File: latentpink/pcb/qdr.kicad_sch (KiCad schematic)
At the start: 68 parts, among them U2 XC7K160T-2FBG484C, U28 IS25WP256D-JLLE, U3 CY7C2245KV18-450BZXI

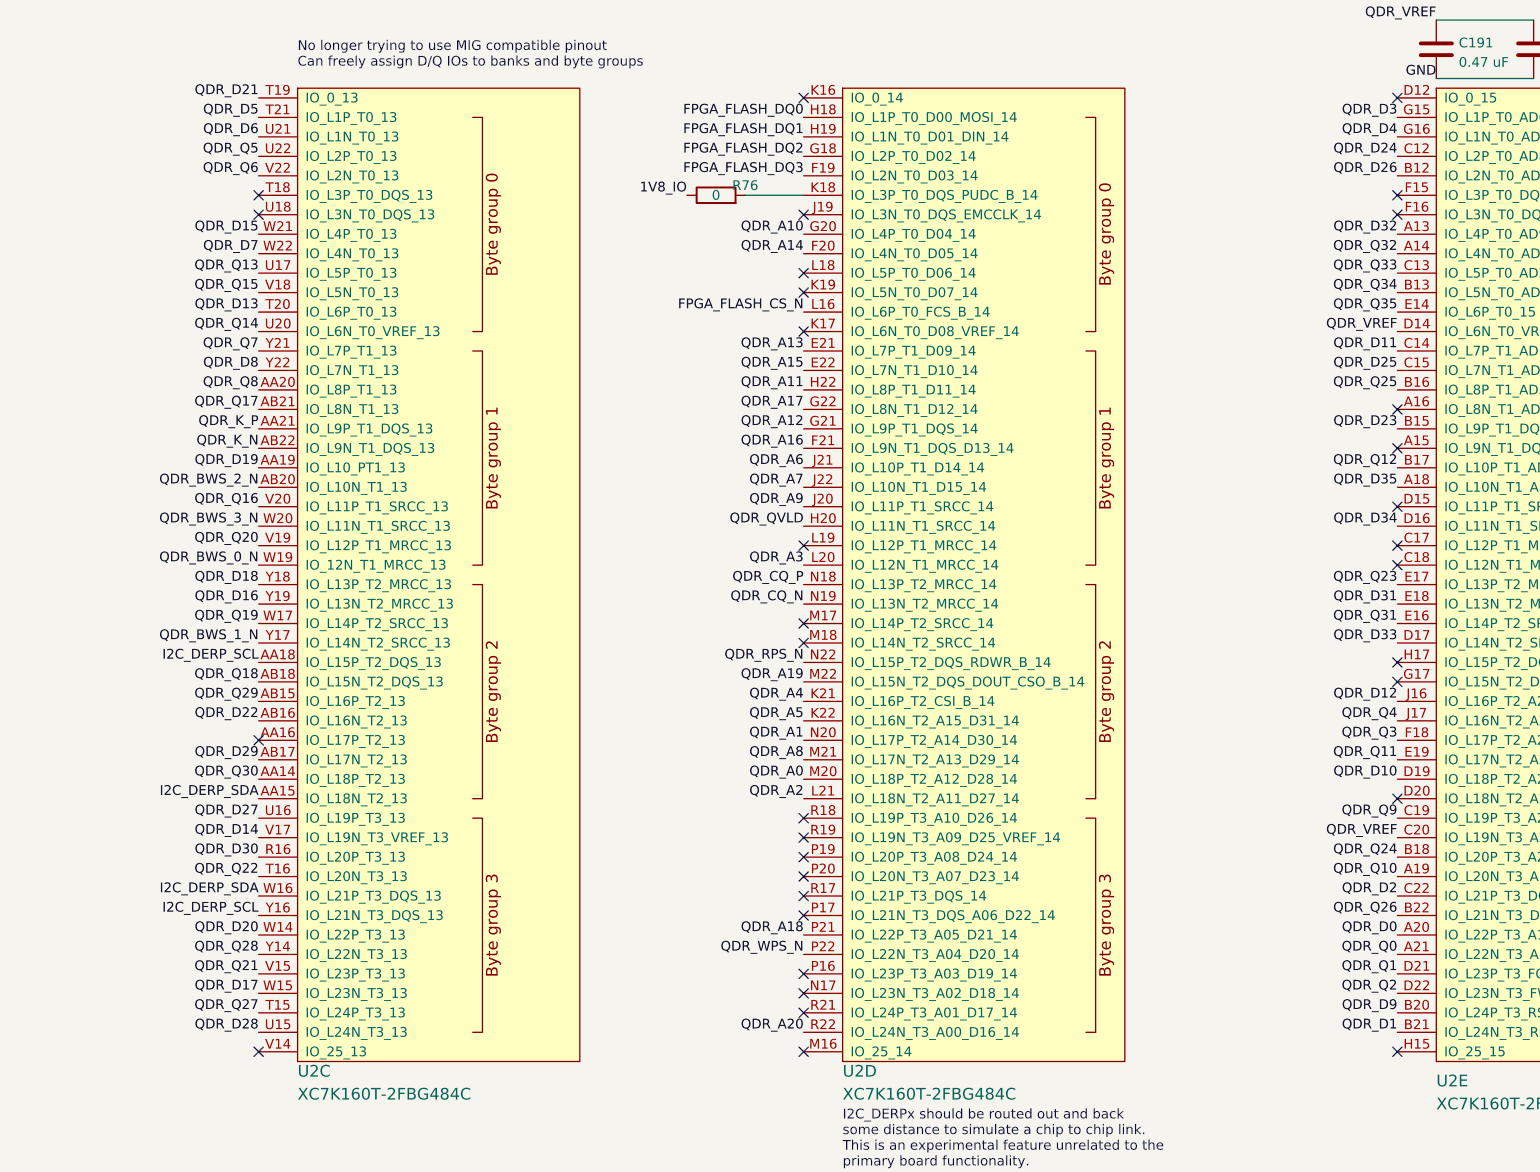
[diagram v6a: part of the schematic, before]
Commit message: Continued initial QDR routing
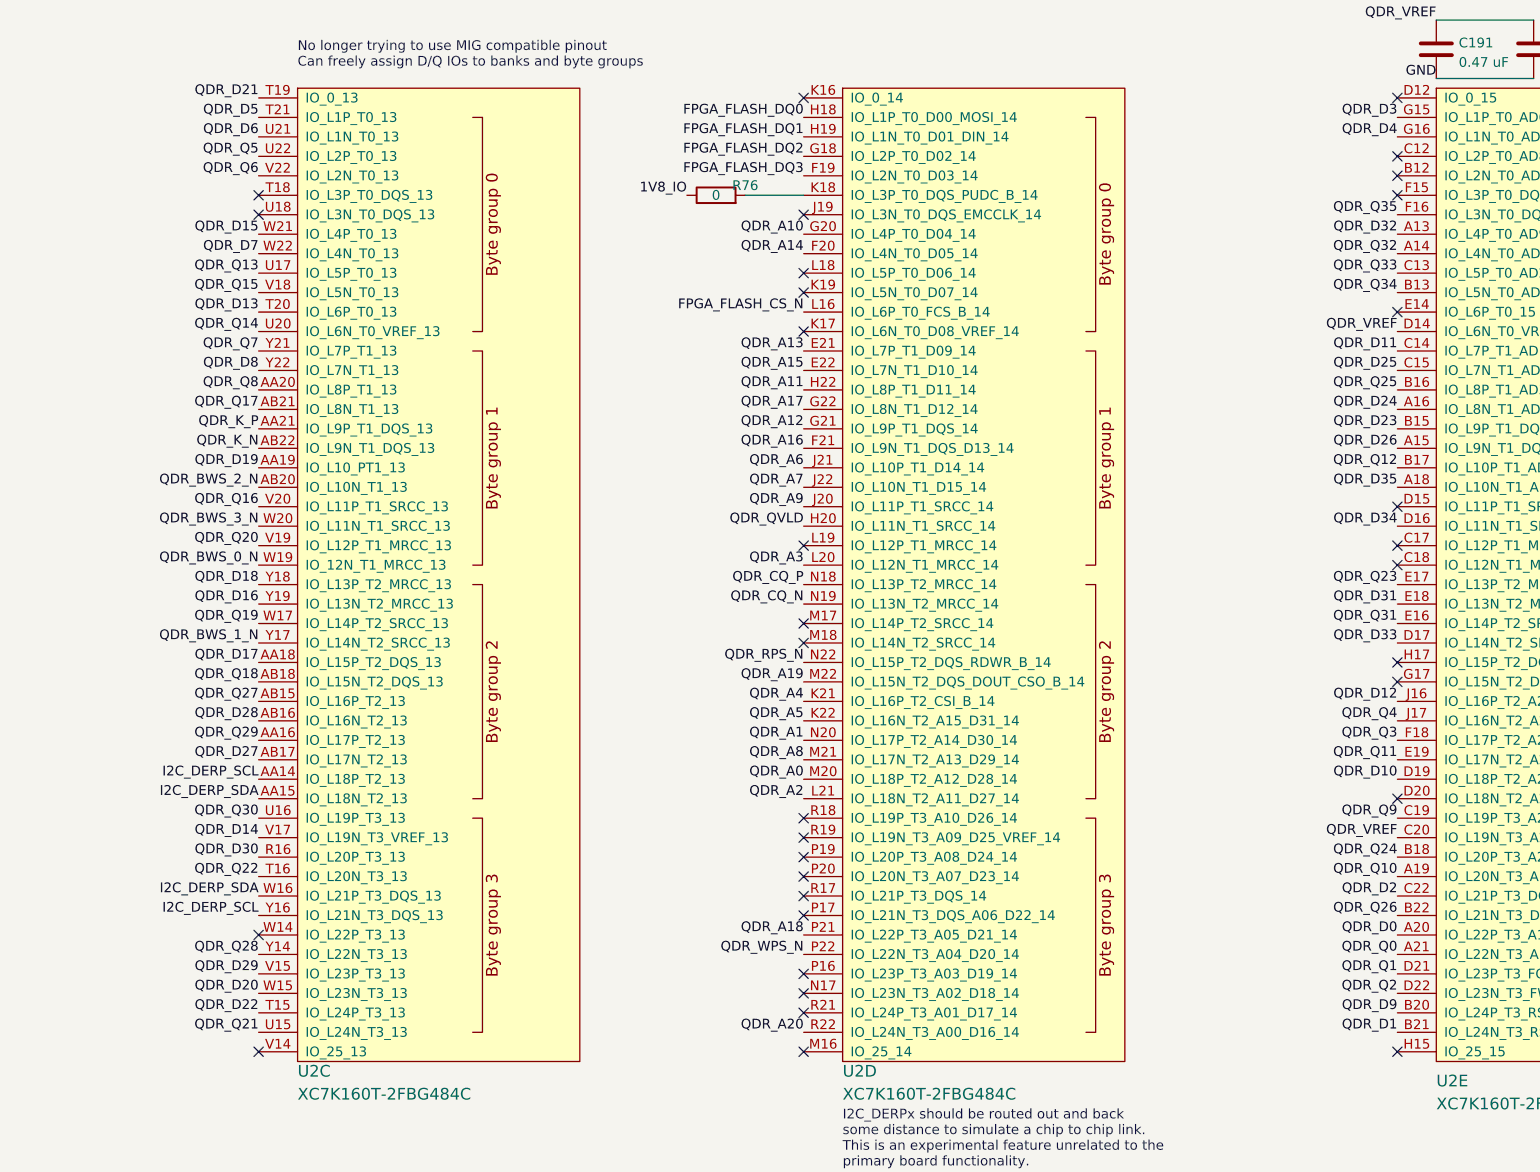
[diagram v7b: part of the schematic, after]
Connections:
- net I2C_DERP_SCL: now also U2.AA14 (IO_L18P_T2_13); no longer U2.AA18 (IO_L15P_T2_DQS_13)
- net QDR_D17: now also U2.AA18 (IO_L15P_T2_DQS_13); no longer U2.W15 (IO_L23N_T3_13)
- net QDR_D20: now also U2.W15 (IO_L23N_T3_13); no longer U2.W14 (IO_L22P_T3_13)
- net QDR_D22: now also U2.T15 (IO_L24P_T3_13); no longer U2.AB16 (IO_L16N_T2_13)
- net QDR_D24: now also U2.A16 (IO_L8N_T1_AD3N_15); no longer U2.C12 (IO_L2P_T0_AD8P_15)
- net QDR_D26: now also U2.A15 (IO_L9N_T1_DQS_AD11N_15); no longer U2.B12 (IO_L2N_T0_AD8N_15)
- net QDR_D27: now also U2.AB17 (IO_L17N_T2_13); no longer U2.U16 (IO_L19P_T3_13)
- net QDR_D28: now also U2.AB16 (IO_L16N_T2_13); no longer U2.U15 (IO_L24N_T3_13)
- net QDR_D29: now also U2.V15 (IO_L23P_T3_13); no longer U2.AB17 (IO_L17N_T2_13)
- net QDR_Q21: now also U2.U15 (IO_L24N_T3_13); no longer U2.V15 (IO_L23P_T3_13)
- net QDR_Q27: now also U2.AB15 (IO_L16P_T2_13); no longer U2.T15 (IO_L24P_T3_13)
- net QDR_Q29: now also U2.AA16 (IO_L17P_T2_13); no longer U2.AB15 (IO_L16P_T2_13)
- net QDR_Q30: now also U2.U16 (IO_L19P_T3_13); no longer U2.AA14 (IO_L18P_T2_13)
- net QDR_Q35: now also U2.F16 (IO_L3N_T0_DQS_AD1N_15); no longer U2.E14 (IO_L6P_T0_15)
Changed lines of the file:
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@@
   (paper "A3")
   (title_block
-    (date "2023-06-01")
+    (date "2023-06-03")
     (rev "0.1")
     (company "Antikernel Labs")
@@
   (no_connect (at 269.24 132.08))
   (no_connect (at 346.71 99.06))
+  (no_connect (at 346.71 33.02))
   (no_connect (at 33.02 181.61))
   (no_connect (at 346.71 25.4))
   (no_connect (at 269.24 83.82))
-  (no_connect (at 346.71 40.64))
   (no_connect (at 346.71 38.1))
   (no_connect (at 269.24 149.86))
@@
   (no_connect (at 346.71 101.6))
   (no_connect (at 346.71 78.74))
-  (no_connect (at 346.71 71.12))
+  (no_connect (at 346.71 53.34))
   (no_connect (at 269.24 55.88))
   (no_connect (at 269.24 25.4))
@@
   (no_connect (at 346.71 149.86))
   (no_connect (at 200.66 264.16))
-  (no_connect (at 346.71 66.04))
   (no_connect (at 269.24 129.54))
   (no_connect (at 33.02 179.07))
@@
   (no_connect (at 269.24 93.98))
   (no_connect (at 269.24 127))
-  (no_connect (at 198.12 109.22))
+  (no_connect (at 346.71 35.56))
+  (no_connect (at 198.12 134.62))
   (wire (pts (xy 88.9 209.55) (xy 101.6 209.55))
     (stroke (width 0) (type default) (color 0 0 0 0))
@@
     (effects (font (size 1.27 1.27)) (justify right bottom))
   )
-  (label "QDR_D20" (at 198.12 134.62 180)
+  (label "QDR_D20" (at 198.12 142.24 180)
     (effects (font (size 1.27 1.27)) (justify right bottom))
   )
@@
     (effects (font (size 1.27 1.27)) (justify right bottom))
   )
-  (label "QDR_D28" (at 198.12 147.32 180)
+  (label "QDR_D28" (at 198.12 106.68 180)
     (effects (font (size 1.27 1.27)) (justify right bottom))
   )
@@
     (effects (font (size 1.27 1.27)) (justify right bottom))
   )
-  (label "QDR_D29" (at 198.12 111.76 180)
+  (label "QDR_D29" (at 198.12 139.7 180)
     (effects (font (size 1.27 1.27)) (justify right bottom))
   )
@@
     (effects (font (size 1.27 1.27)) (justify right bottom))
   )
-  (label "QDR_Q30" (at 198.12 114.3 180)
+  (label "QDR_Q30" (at 198.12 119.38 180)
     (effects (font (size 1.27 1.27)) (justify right bottom))
   )
@@
     (effects (font (size 1.27 1.27)) (justify right bottom))
   )
-  (label "QDR_D17" (at 198.12 142.24 180)
+  (label "QDR_D17" (at 198.12 99.06 180)
     (effects (font (size 1.27 1.27)) (justify right bottom))
   )
@@
     (effects (font (size 1.27 1.27)) (justify right bottom))
   )
-  (label "QDR_D27" (at 198.12 119.38 180)
+  (label "QDR_D27" (at 198.12 111.76 180)
     (effects (font (size 1.27 1.27)) (justify right bottom))
   )
@@
     (effects (font (size 1.27 1.27)) (justify right bottom))
   )
-  (label "QDR_Q29" (at 198.12 104.14 180)
+  (label "QDR_Q29" (at 198.12 109.22 180)
     (effects (font (size 1.27 1.27)) (justify right bottom))
   )
@@
     (effects (font (size 1.27 1.27)) (justify right bottom))
   )
-  (label "QDR_D26" (at 346.71 35.56 180)
+  (label "QDR_D26" (at 346.71 71.12 180)
     (effects (font (size 1.27 1.27)) (justify right bottom))
   )
@@
     (effects (font (size 1.27 1.27)) (justify right bottom))
   )
-  (label "QDR_D24" (at 346.71 33.02 180)
+  (label "QDR_D24" (at 346.71 66.04 180)
     (effects (font (size 1.27 1.27)) (justify right bottom))
   )
@@
     (effects (font (size 1.27 1.27)) (justify right bottom))
   )
-  (label "QDR_Q21" (at 198.12 139.7 180)
+  (label "QDR_Q21" (at 198.12 147.32 180)
     (effects (font (size 1.27 1.27)) (justify right bottom))
   )
@@
     (effects (font (size 1.27 1.27)) (justify right bottom))
   )
-  (label "QDR_Q27" (at 198.12 144.78 180)
+  (label "QDR_Q27" (at 198.12 104.14 180)
     (effects (font (size 1.27 1.27)) (justify right bottom))
   )
@@
     (effects (font (size 1.27 1.27)) (justify right bottom))
   )
-  (label "QDR_D22" (at 198.12 106.68 180)
+  (label "QDR_D22" (at 198.12 144.78 180)
     (effects (font (size 1.27 1.27)) (justify right bottom))
   )
@@
     (effects (font (size 1.27 1.27)) (justify right bottom))
   )
-  (label "QDR_Q35" (at 346.71 53.34 180)
+  (label "QDR_Q35" (at 346.71 40.64 180)
     (effects (font (size 1.27 1.27)) (justify right bottom))
   )
@@
     (effects (font (size 1.27 1.27)) (justify right bottom))
   )
-  (label "I2C_DERP_SCL" (at 198.12 99.06 180)
-    (effects (font (size 1.27 1.27)) (justify right bottom))
-  )
+  (label "I2C_DERP_SCL" (at 198.12 114.3 180)
+    (effects (font (size 1.27 1.27)) (justify right bottom))
+  )

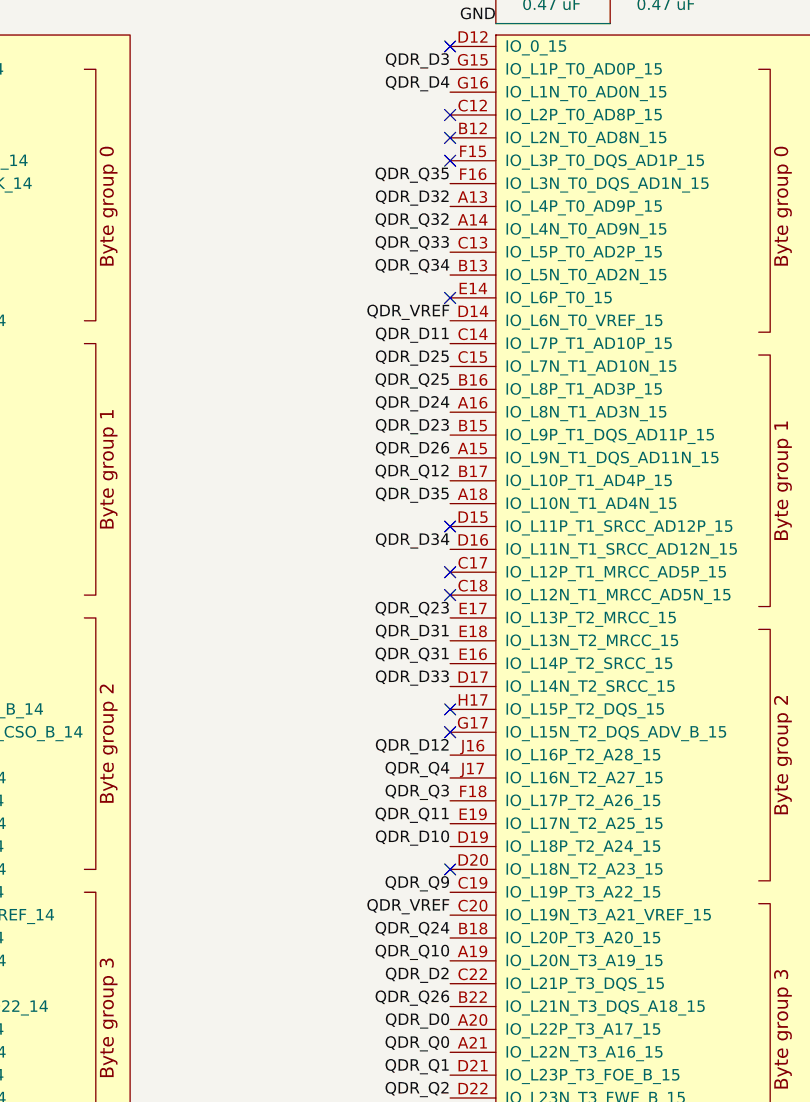
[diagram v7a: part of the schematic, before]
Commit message: Finished initial QDR routing, not length matched. 74 unrouted.
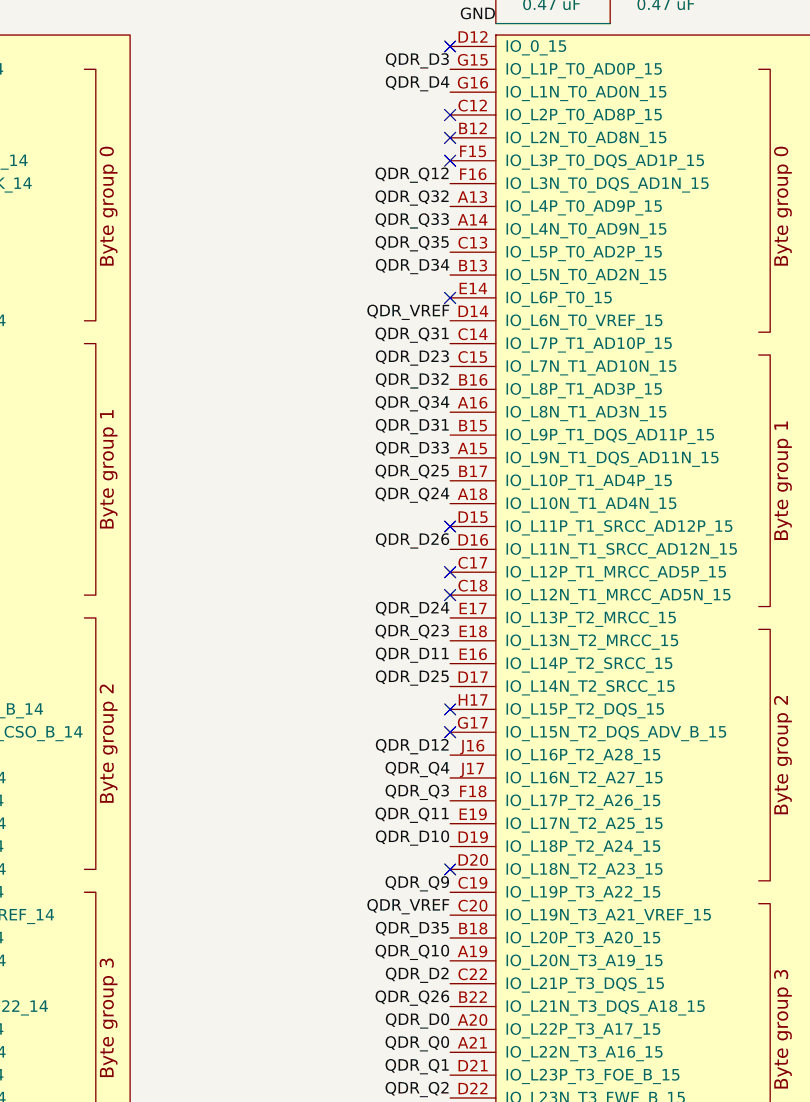
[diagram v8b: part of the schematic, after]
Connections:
- net QDR_D11: now also U2.E16 (IO_L14P_T2_SRCC_15); no longer U2.C14 (IO_L7P_T1_AD10P_15)
- net QDR_D23: now also U2.C15 (IO_L7N_T1_AD10N_15); no longer U2.B15 (IO_L9P_T1_DQS_AD11P_15)
- net QDR_D24: now also U2.E17 (IO_L13P_T2_MRCC_15); no longer U2.A16 (IO_L8N_T1_AD3N_15)
- net QDR_D25: now also U2.D17 (IO_L14N_T2_SRCC_15); no longer U2.C15 (IO_L7N_T1_AD10N_15)
- net QDR_D26: now also U2.D16 (IO_L11N_T1_SRCC_AD12N_15); no longer U2.A15 (IO_L9N_T1_DQS_AD11N_15)
- net QDR_D31: now also U2.B15 (IO_L9P_T1_DQS_AD11P_15); no longer U2.E18 (IO_L13N_T2_MRCC_15)
- net QDR_D32: now also U2.B16 (IO_L8P_T1_AD3P_15); no longer U2.A13 (IO_L4P_T0_AD9P_15)
- net QDR_D33: now also U2.A15 (IO_L9N_T1_DQS_AD11N_15); no longer U2.D17 (IO_L14N_T2_SRCC_15)
- net QDR_D34: now also U2.B13 (IO_L5N_T0_AD2N_15); no longer U2.D16 (IO_L11N_T1_SRCC_AD12N_15)
- net QDR_D35: now also U2.B18 (IO_L20P_T3_A20_15); no longer U2.A18 (IO_L10N_T1_AD4N_15)
- net QDR_Q12: now also U2.F16 (IO_L3N_T0_DQS_AD1N_15); no longer U2.B17 (IO_L10P_T1_AD4P_15)
- net QDR_Q23: now also U2.E18 (IO_L13N_T2_MRCC_15); no longer U2.E17 (IO_L13P_T2_MRCC_15)
- net QDR_Q24: now also U2.A18 (IO_L10N_T1_AD4N_15); no longer U2.B18 (IO_L20P_T3_A20_15)
- net QDR_Q25: now also U2.B17 (IO_L10P_T1_AD4P_15); no longer U2.B16 (IO_L8P_T1_AD3P_15)
- net QDR_Q31: now also U2.C14 (IO_L7P_T1_AD10P_15); no longer U2.E16 (IO_L14P_T2_SRCC_15)
- net QDR_Q32: now also U2.A13 (IO_L4P_T0_AD9P_15); no longer U2.A14 (IO_L4N_T0_AD9N_15)
- net QDR_Q33: now also U2.A14 (IO_L4N_T0_AD9N_15); no longer U2.C13 (IO_L5P_T0_AD2P_15)
- net QDR_Q34: now also U2.A16 (IO_L8N_T1_AD3N_15); no longer U2.B13 (IO_L5N_T0_AD2N_15)
- net QDR_Q35: now also U2.C13 (IO_L5P_T0_AD2P_15); no longer U2.F16 (IO_L3N_T0_DQS_AD1N_15)
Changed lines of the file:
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@@
     (effects (font (size 1.27 1.27)) (justify right bottom))
   )
-  (label "QDR_D31" (at 346.71 91.44 180)
+  (label "QDR_D31" (at 346.71 68.58 180)
     (effects (font (size 1.27 1.27)) (justify right bottom))
   )
@@
     (effects (font (size 1.27 1.27)) (justify right bottom))
   )
-  (label "QDR_D32" (at 346.71 43.18 180)
+  (label "QDR_D32" (at 346.71 63.5 180)
     (effects (font (size 1.27 1.27)) (justify right bottom))
   )
@@
     (effects (font (size 1.27 1.27)) (justify right bottom))
   )
-  (label "QDR_D35" (at 346.71 76.2 180)
+  (label "QDR_D35" (at 346.71 124.46 180)
     (effects (font (size 1.27 1.27)) (justify right bottom))
   )
@@
     (effects (font (size 1.27 1.27)) (justify right bottom))
   )
-  (label "QDR_Q12" (at 346.71 73.66 180)
+  (label "QDR_Q12" (at 346.71 40.64 180)
     (effects (font (size 1.27 1.27)) (justify right bottom))
   )
@@
     (effects (font (size 1.27 1.27)) (justify right bottom))
   )
-  (label "QDR_Q32" (at 346.71 45.72 180)
-    (effects (font (size 1.27 1.27)) (justify right bottom))
-  )
-  (label "QDR_D34" (at 346.71 81.28 180)
+  (label "QDR_Q32" (at 346.71 43.18 180)
+    (effects (font (size 1.27 1.27)) (justify right bottom))
+  )
+  (label "QDR_D34" (at 346.71 50.8 180)
     (effects (font (size 1.27 1.27)) (justify right bottom))
   )
@@
     (effects (font (size 1.27 1.27)) (justify right bottom))
   )
-  (label "QDR_Q34" (at 346.71 50.8 180)
+  (label "QDR_Q34" (at 346.71 66.04 180)
     (effects (font (size 1.27 1.27)) (justify right bottom))
   )
@@
     (effects (font (size 1.27 1.27)) (justify right bottom))
   )
-  (label "QDR_Q24" (at 346.71 124.46 180)
+  (label "QDR_Q24" (at 346.71 76.2 180)
     (effects (font (size 1.27 1.27)) (justify right bottom))
   )
@@
     (effects (font (size 1.27 1.27)) (justify right bottom))
   )
-  (label "QDR_D26" (at 346.71 71.12 180)
+  (label "QDR_D26" (at 346.71 81.28 180)
     (effects (font (size 1.27 1.27)) (justify right bottom))
   )
@@
     (effects (font (size 1.27 1.27)) (justify right bottom))
   )
-  (label "QDR_Q23" (at 346.71 88.9 180)
+  (label "QDR_Q23" (at 346.71 91.44 180)
     (effects (font (size 1.27 1.27)) (justify right bottom))
   )
@@
     (effects (font (size 1.27 1.27)) (justify right bottom))
   )
-  (label "QDR_D24" (at 346.71 66.04 180)
+  (label "QDR_D24" (at 346.71 88.9 180)
     (effects (font (size 1.27 1.27)) (justify right bottom))
   )
@@
     (effects (font (size 1.27 1.27)) (justify right bottom))
   )
-  (label "QDR_D23" (at 346.71 68.58 180)
+  (label "QDR_D23" (at 346.71 60.96 180)
     (effects (font (size 1.27 1.27)) (justify right bottom))
   )
@@
     (effects (font (size 1.27 1.27)) (justify right bottom))
   )
-  (label "QDR_Q25" (at 346.71 63.5 180)
+  (label "QDR_Q25" (at 346.71 73.66 180)
     (effects (font (size 1.27 1.27)) (justify right bottom))
   )
@@
     (effects (font (size 1.27 1.27)) (justify right bottom))
   )
-  (label "QDR_Q33" (at 346.71 48.26 180)
-    (effects (font (size 1.27 1.27)) (justify right bottom))
-  )
-  (label "QDR_D33" (at 346.71 96.52 180)
+  (label "QDR_Q33" (at 346.71 45.72 180)
+    (effects (font (size 1.27 1.27)) (justify right bottom))
+  )
+  (label "QDR_D33" (at 346.71 71.12 180)
     (effects (font (size 1.27 1.27)) (justify right bottom))
   )
@@
     (effects (font (size 1.27 1.27)) (justify right bottom))
   )
-  (label "QDR_D25" (at 346.71 60.96 180)
+  (label "QDR_D25" (at 346.71 96.52 180)
     (effects (font (size 1.27 1.27)) (justify right bottom))
   )
@@
     (effects (font (size 1.27 1.27)) (justify right bottom))
   )
-  (label "QDR_Q35" (at 346.71 40.64 180)
+  (label "QDR_Q35" (at 346.71 48.26 180)
     (effects (font (size 1.27 1.27)) (justify right bottom))
   )
@@
     (effects (font (size 1.27 1.27)) (justify right bottom))
   )
-  (label "QDR_D11" (at 346.71 58.42 180)
+  (label "QDR_D11" (at 346.71 93.98 180)
     (effects (font (size 1.27 1.27)) (justify right bottom))
   )
@@
     (effects (font (size 1.27 1.27)) (justify right bottom))
   )
-  (label "QDR_Q31" (at 346.71 93.98 180)
-    (effects (font (size 1.27 1.27)) (justify right bottom))
-  )
+  (label "QDR_Q31" (at 346.71 58.42 180)
+    (effects (font (size 1.27 1.27)) (justify right bottom))
+  )
